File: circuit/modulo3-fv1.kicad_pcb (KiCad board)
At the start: 2 copper layers, 84 x 52 mm, 57 parts, among them J2 HOLE, J4 HOLE, J5 HOLE, J7 HOLE, U1 OPA1642, U10 TLE2426, U2 FV1_CONN, U3 FV-1, U4 POWER, U5 LM1117 3V3, U6 DIFFAUDIO, U7 AD5142A, U8 AMPCTRL, U9 PREAMP, Y1 32768Hz

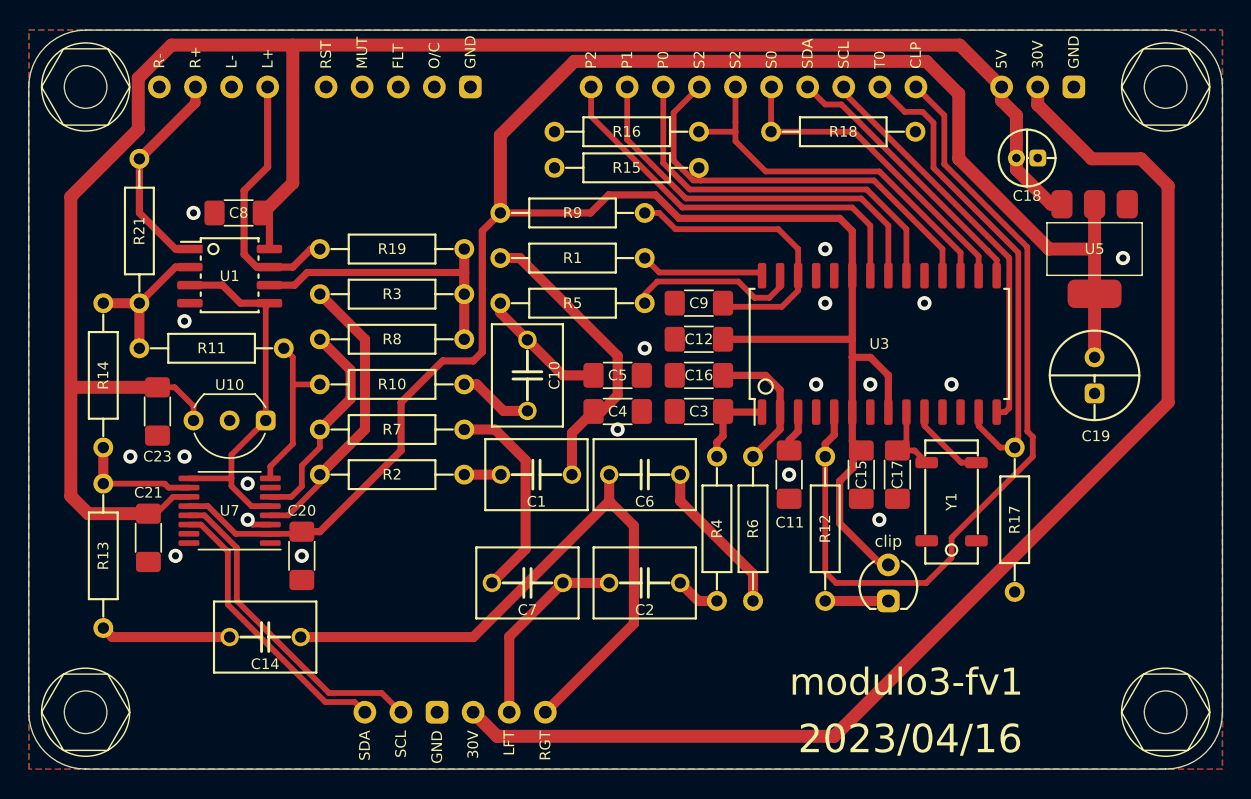
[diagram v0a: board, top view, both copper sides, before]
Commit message: lowered the watch resolution to .24 ms; moved the pins of the display; added pull-ups for mix i2c
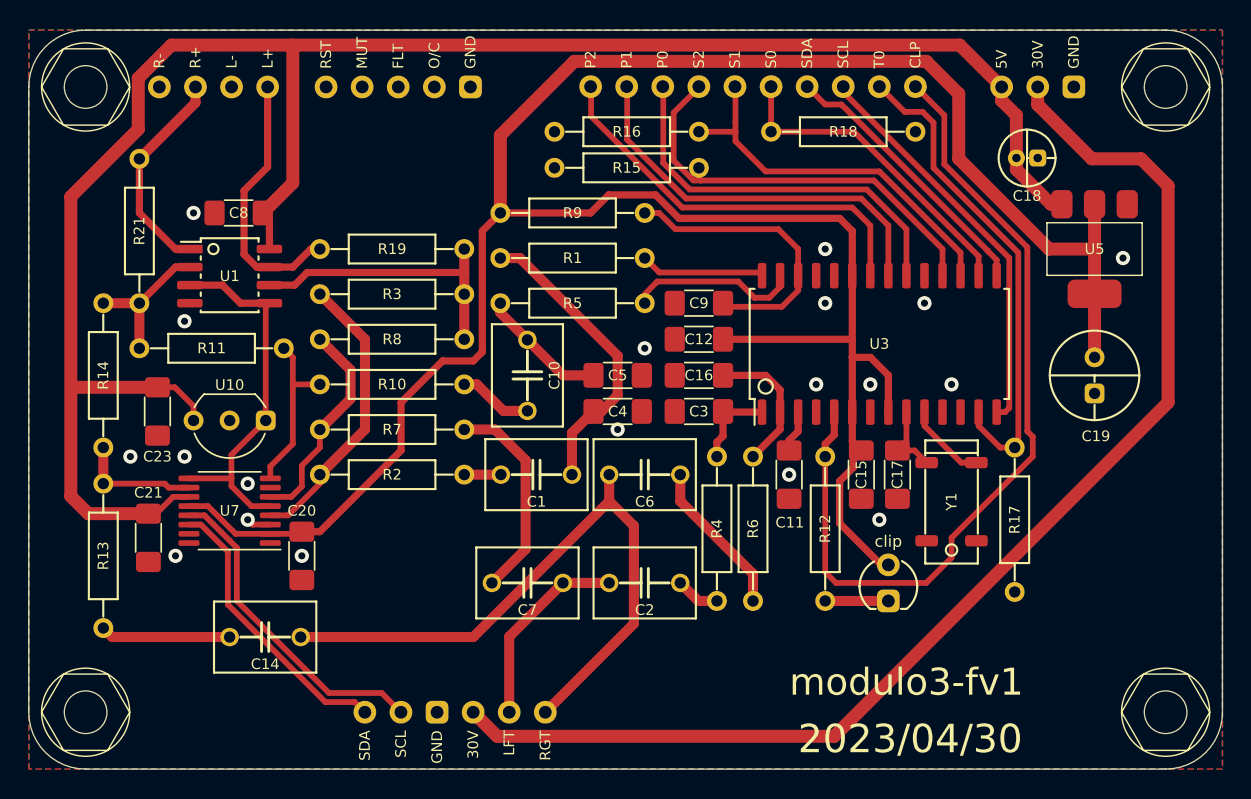
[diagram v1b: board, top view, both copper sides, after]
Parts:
- U4: value POWER -> PWR_CONN
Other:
- board text added: "2023/04/30"
- board text removed: "2023/04/16"
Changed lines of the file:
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@@
+    )
+  )
+  (footprint "myAmp:FV1_CONN" (layer "F.Cu")
+    (at 100.965 53.975)
+    (property "Sheetfile" "modulo3-fv1.kicad_sch")
+    (property "Sheetname" "")
+    (attr through_hole)
+    (fp_text reference "U2" (at 0 -12.7 unlocked) (layer "F.SilkS") hide
+        (effects (font (size 0.75 0.75) (thickness 0.15)))
+    )
+    (fp_text value "FV1_CONN" (at 0 1 unlocked) (layer "F.Fab") hide
+        (effects (font (size 0.75 0.75) (thickness 0.15)))
+    )
+    (fp_text user "P1" (at -8.89 -1.27 90 unlocked) (layer "F.SilkS")
+        (effects (font (size 0.75 0.75) (thickness 0.15)) (justify left))
+    )
+    (fp_text user "S0" (at 1.27 -1.27 90 unlocked) (layer "F.SilkS")
+        (effects (font (size 0.75 0.75) (thickness 0.15)) (justify left))
+    )
+    (fp_text user "P0" (at -6.35 -1.27 90 unlocked) (layer "F.SilkS")
+        (effects (font (size 0.75 0.75) (thickness 0.15)) (justify left))
+    )
+    (fp_text user "S1" (at -1.27 -1.27 90 unlocked) (layer "F.SilkS")
+        (effects (font (size 0.75 0.75) (thickness 0.15)) (justify left))
+    )
+    (fp_text user "CLP" (at 11.43 -1.27 90 unlocked) (layer "F.SilkS")
+        (effects (font (size 0.75 0.75) (thickness 0.15)) (justify left))
+    )
+    (fp_text user "P2" (at -11.43 -1.27 90 unlocked) (layer "F.SilkS")
+        (effects (font (size 0.75 0.75) (thickness 0.15)) (justify left))
+    )
+    (fp_text user "T0" (at 8.89 -1.27 90 unlocked) (layer "F.SilkS")
+        (effects (font (size 0.75 0.75) (thickness 0.15)) (justify left))
+    )
+    (fp_text user "SCL" (at 6.35 -1.27 90 unlocked) (layer "F.SilkS")
+        (effects (font (size 0.75 0.75) (thickness 0.15)) (justify left))
+    )
+    (fp_text user "SDA" (at 3.81 -1.27 90 unlocked) (layer "F.SilkS")
+        (effects (font (size 0.75 0.75) (thickness 0.15)) (justify left))
+    )
+    (fp_text user "S2" (at -3.81 -1.27 90 unlocked) (layer "F.SilkS")
+        (effects (font (size 0.75 0.75) (thickness 0.15)) (justify left))
+    )
+    (pad "1" thru_hole circle (at -11.43 0) (size 1.6 1.6) (drill 0.9) (layers "*.Cu" "*.Mask")
+      (net 24 "/POT2") (pinfunction "POT2") (pintype "input"))
+    (pad "2" thru_hole circle (at -8.89 0) (size 1.6 1.6) (drill 0.9) (layers "*.Cu" "*.Mask")
+      (net 23 "/POT1") (pinfunction "POT1") (pintype "input"))
+    (pad "3" thru_hole circle (at -6.35 0) (size 1.6 1.6) (drill 0.9) (layers "*.Cu" "*.Mask")
+      (net 22 "/POT0") (pinfunction "POT0") (pintype "input"))
+    (pad "4" thru_hole circle (at -3.81 0) (size 1.6 1.6) (drill 0.9) (layers "*.Cu" "*.Mask")
+      (net 27 "/S2") (pinfunction "S2") (pintype "input"))
+    (pad "5" thru_hole circle (at -1.27 0) (size 1.6 1.6) (drill 0.9) (layers "*.Cu" "*.Mask")
+      (net 26 "/S1") (pinfunction "S1") (pintype "input"))
+    (pad "6" thru_hole circle (at 1.27 0) (size 1.6 1.6) (drill 0.9) (layers "*.Cu" "*.Mask")
+      (net 25 "/S0") (pinfunction "S0") (pintype "input"))
+    (pad "7" thru_hole circle (at 3.81 0) (size 1.6 1.6) (drill 0.9) (layers "*.Cu" "*.Mask")
+      (net 29 "/FV_SDA") (pinfunction "SDA") (pintype "input"))
+    (pad "8" thru_hole circle (at 6.35 0) (size 1.6 1.6) (drill 0.9) (layers "*.Cu" "*.Mask")
+      (net 30 "/FV_SCL") (pinfunction "SCL") (pintype "input"))
+    (pad "9" thru_hole circle (at 8.89 0) (size 1.6 1.6) (drill 0.9) (layers "*.Cu" "*.Mask")
+      (net 28 "/T0") (pinfunction "T0") (pintype "input"))
+    (pad "10" thru_hole circle (at 11.43 0) (size 1.6 1.6) (drill 0.9) (layers "*.Cu" "*.Mask")
+      (net 42 "/CLIP") (pinfunction "CLP") (pintype "input"))
+    (model "${KIPRJMOD}/myAmp.pretty/models/PinHeader_1x10_P2.54mm_Vertical.step"
+      (offset (xyz 11.43 0 0))
+      (scale (xyz 1 1 1))
+      (rotate (xyz 0 0 90))
     )
   )
@@
         (effects (font (size 0.75 0.75) (thickness 0.15)))
     )
-    (fp_text value "POWER" (at 2.54 -0.635) (layer "F.Fab") hide
+    (fp_text value "PWR_CONN" (at 2.54 -0.635) (layer "F.Fab") hide
         (effects (font (size 0.03 0.03) (thickness 0.0075)))
     )
@@
       (scale (xyz 1 1 1))
       (rotate (xyz 0 0 0))
-    )
-  )
-  (footprint "myAmp:FV1_CONN" (layer "F.Cu")
-    (at 101 54)
-    (property "Sheetfile" "modulo3-fv1.kicad_sch")
-    (property "Sheetname" "")
-    (attr through_hole)
-    (fp_text reference "U2" (at 0 -12.7 unlocked) (layer "F.SilkS") hide
-        (effects (font (size 0.75 0.75) (thickness 0.15)))
-    )
-    (fp_text value "FV1_CONN" (at 0 1 unlocked) (layer "F.Fab") hide
-        (effects (font (size 0.75 0.75) (thickness 0.15)))
-    )
-    (fp_text user "T0" (at 8.89 -1.27 90 unlocked) (layer "F.SilkS")
-        (effects (font (size 0.75 0.75) (thickness 0.15)) (justify left))
-    )
-    (fp_text user "S2" (at -1.27 -1.27 90 unlocked) (layer "F.SilkS")
-        (effects (font (size 0.75 0.75) (thickness 0.15)) (justify left))
-    )
-    (fp_text user "SDA" (at 3.81 -1.27 90 unlocked) (layer "F.SilkS")
-        (effects (font (size 0.75 0.75) (thickness 0.15)) (justify left))
-    )
-    (fp_text user "S2" (at -3.81 -1.27 90 unlocked) (layer "F.SilkS")
-        (effects (font (size 0.75 0.75) (thickness 0.15)) (justify left))
-    )
-    (fp_text user "P1" (at -8.89 -1.27 90 unlocked) (layer "F.SilkS")
-        (effects (font (size 0.75 0.75) (thickness 0.15)) (justify left))
-    )
-    (fp_text user "P2" (at -11.43 -1.27 90 unlocked) (layer "F.SilkS")
-        (effects (font (size 0.75 0.75) (thickness 0.15)) (justify left))
-    )
-    (fp_text user "SCL" (at 6.35 -1.27 90 unlocked) (layer "F.SilkS")
-        (effects (font (size 0.75 0.75) (thickness 0.15)) (justify left))
-    )
-    (fp_text user "S0" (at 1.27 -1.27 90 unlocked) (layer "F.SilkS")
-        (effects (font (size 0.75 0.75) (thickness 0.15)) (justify left))
-    )
-    (fp_text user "P0" (at -6.35 -1.27 90 unlocked) (layer "F.SilkS")
-        (effects (font (size 0.75 0.75) (thickness 0.15)) (justify left))
-    )
-    (fp_text user "CLP" (at 11.43 -1.27 90 unlocked) (layer "F.SilkS")
-        (effects (font (size 0.75 0.75) (thickness 0.15)) (justify left))
-    )
-    (pad "1" thru_hole circle (at -11.43 0) (size 1.6 1.6) (drill 0.9) (layers "*.Cu" "*.Mask")
-      (net 24 "/POT2") (pinfunction "POT2") (pintype "input"))
-    (pad "2" thru_hole circle (at -8.89 0) (size 1.6 1.6) (drill 0.9) (layers "*.Cu" "*.Mask")
-      (net 23 "/POT1") (pinfunction "POT1") (pintype "input"))
-    (pad "3" thru_hole circle (at -6.35 0) (size 1.6 1.6) (drill 0.9) (layers "*.Cu" "*.Mask")
-      (net 22 "/POT0") (pinfunction "POT0") (pintype "input"))
-    (pad "4" thru_hole circle (at -3.81 0) (size 1.6 1.6) (drill 0.9) (layers "*.Cu" "*.Mask")
-      (net 27 "/S2") (pinfunction "S2") (pintype "input"))
-    (pad "5" thru_hole circle (at -1.27 0) (size 1.6 1.6) (drill 0.9) (layers "*.Cu" "*.Mask")
-      (net 26 "/S1") (pinfunction "S1") (pintype "input"))
-    (pad "6" thru_hole circle (at 1.27 0) (size 1.6 1.6) (drill 0.9) (layers "*.Cu" "*.Mask")
-      (net 25 "/S0") (pinfunction "S0") (pintype "input"))
-    (pad "7" thru_hole circle (at 3.81 0) (size 1.6 1.6) (drill 0.9) (layers "*.Cu" "*.Mask")
-      (net 29 "/FV_SDA") (pinfunction "SDA") (pintype "input"))
-    (pad "8" thru_hole circle (at 6.35 0) (size 1.6 1.6) (drill 0.9) (layers "*.Cu" "*.Mask")
-      (net 30 "/FV_SCL") (pinfunction "SCL") (pintype "input"))
-    (pad "9" thru_hole circle (at 8.89 0) (size 1.6 1.6) (drill 0.9) (layers "*.Cu" "*.Mask")
-      (net 28 "/T0") (pinfunction "T0") (pintype "input"))
-    (pad "10" thru_hole circle (at 11.43 0) (size 1.6 1.6) (drill 0.9) (layers "*.Cu" "*.Mask")
-      (net 42 "/CLIP") (pinfunction "CLP") (pintype "input"))
-    (model "${KIPRJMOD}/myAmp.pretty/models/PinHeader_1x10_P2.54mm_Vertical.step"
-      (offset (xyz 11.43 0 0))
-      (scale (xyz 1 1 1))
-      (rotate (xyz 0 0 90))
     )
   )
@@
     (effects (font (size 1.9 1.9) (thickness 0.3)))
   )
-  (gr_text "2023/04/16" (at 112.03 99.885) (layer "F.SilkS")
+  (gr_text "2023/04/30" (at 112.03 99.885) (layer "F.SilkS")
     (effects (font (size 2 2) (thickness 0.3)))
   )
